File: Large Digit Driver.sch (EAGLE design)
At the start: 25 parts, among them U1 TPIC6B595PTH

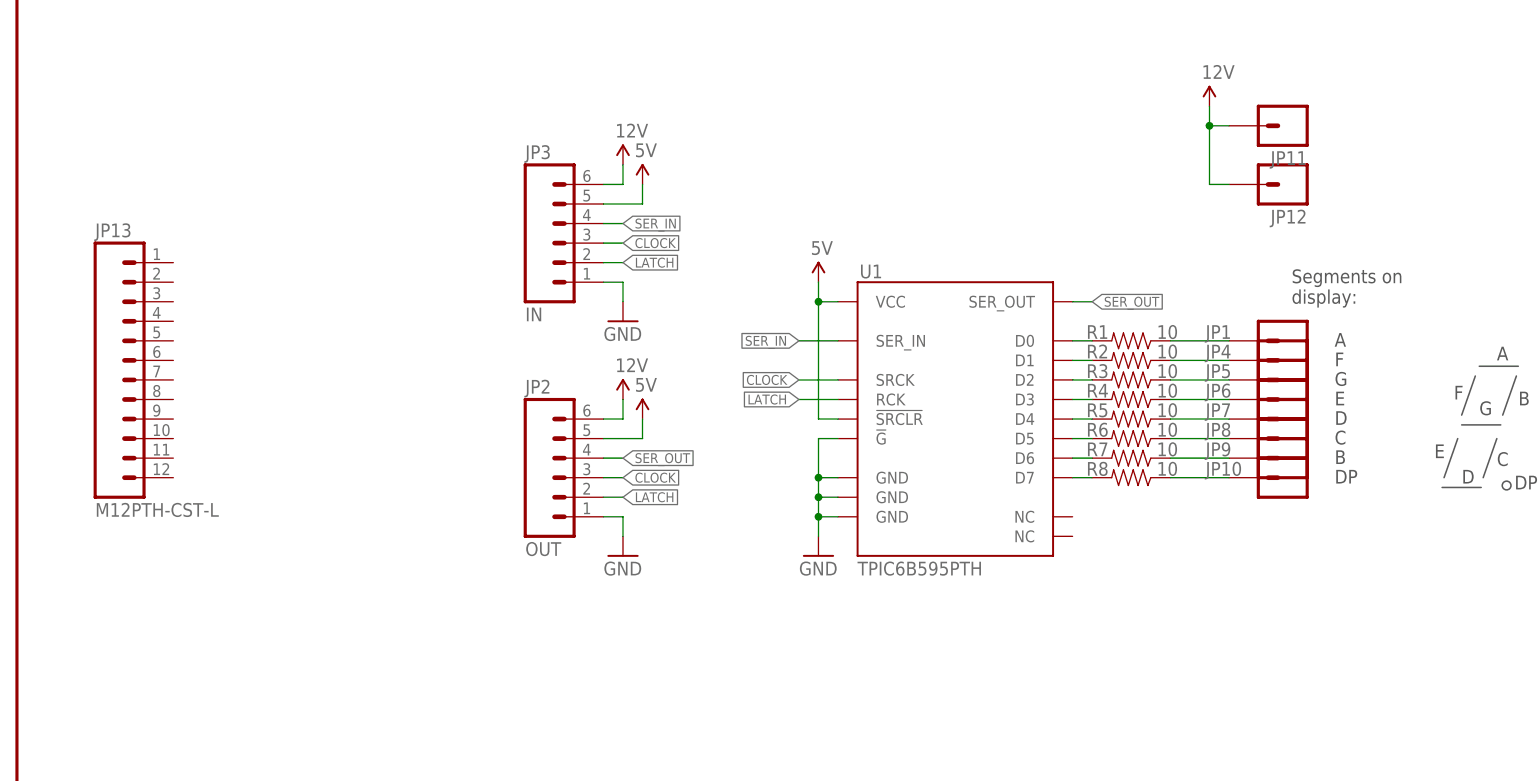
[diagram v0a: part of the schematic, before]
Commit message: Conversion to SMD parts.
Board is much smaller. Uses TPIC6C596.
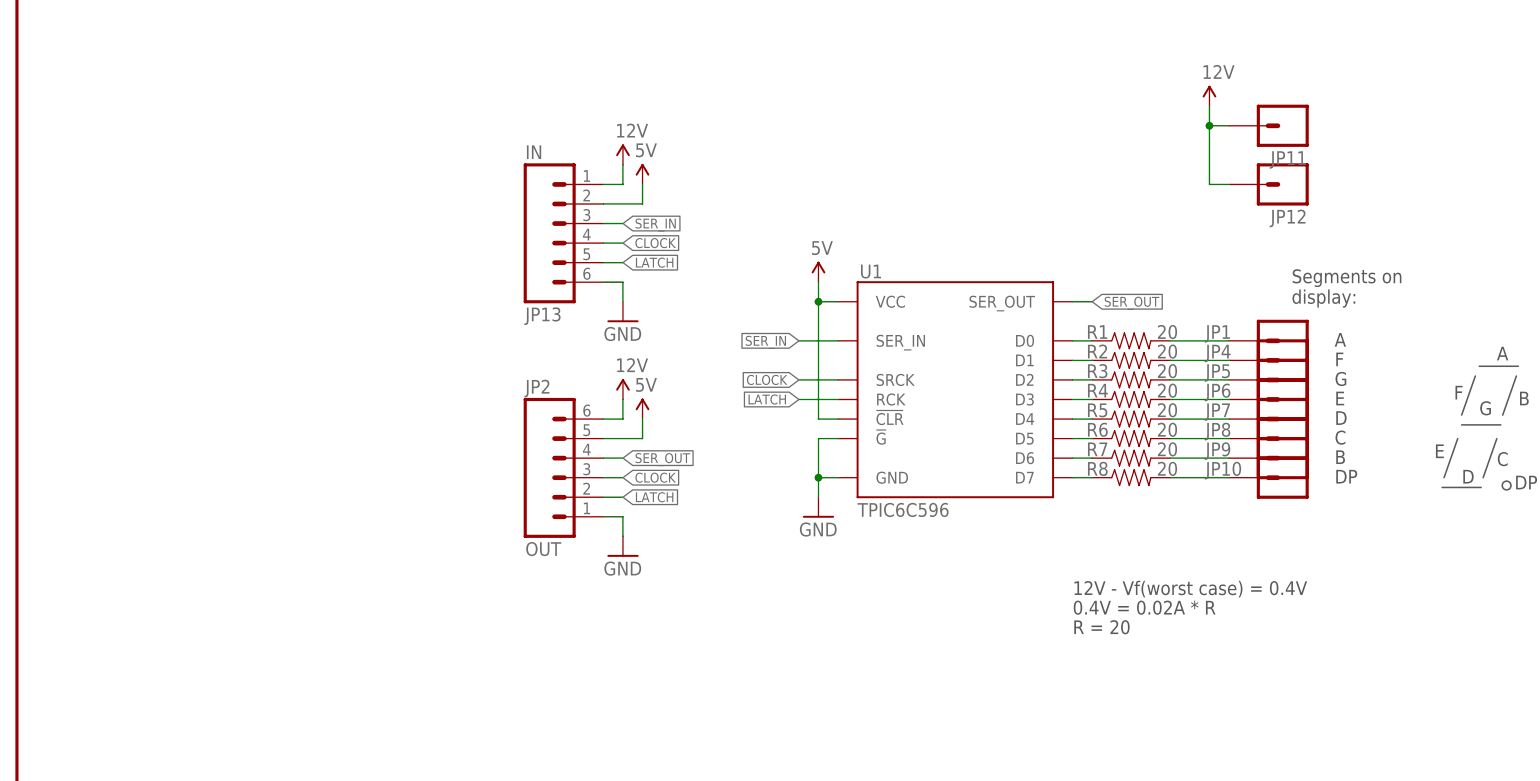
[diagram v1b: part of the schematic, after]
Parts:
- removed JP3: IN, SparkFun-Connectors:M06SILK_FEMALE_PTH
- JP13: value M12PTH-CST-L -> IN; device Spark:M12PTH-CST-L -> SparkFun-Connectors:M06SMD
- JP2: device SparkFun-Connectors:M06SILK_FEMALE_PTH -> SparkFun-Connectors:M06SMD
- R1, R2, R3, R4, R5, R6, R7, R8: value 10 -> 20; device SparkFun-Resistors:1KOHM-1/4W-1%(PTH) -> SparkFun-Resistors:20OHM1/10W1%(0603)SMD
- U1: value TPIC6B595PTH -> TPIC6C596; device SparkFun-DigitalIC:TPIC6B595PTH -> SparkFun-DigitalIC:TPIC6C596SOIC
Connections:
- net 12V: now also JP13.1; no longer JP3.6
- net 5V: now also JP13.2, U1.!CLR; no longer JP3.5, U1.!SRCLR
- net CLOCK: now also JP13.4; no longer JP3.3
- net D0: now also R1.1; no longer R1.2
- net D1: now also R2.1; no longer R2.2
- net D2: now also R3.1; no longer R3.2
- net D3: now also R4.1; no longer R4.2
- net D4: now also R5.1; no longer R5.2
- net D5: now also R6.1; no longer R6.2
- net D6: now also R7.1; no longer R7.2
- net D7: now also R8.1; no longer R8.2
- net GND: now also JP13.6, U1.GND; no longer JP3.1, U1.GND@10, U1.GND@11, U1.GND@19
- net LATCH: now also JP13.5; no longer JP3.2
- net S0: now also R1.2; no longer R1.1
- net S1: now also R2.2; no longer R2.1
- net S2: now also R3.2; no longer R3.1
- net S3: now also R4.2; no longer R4.1
- net S4: now also R5.2; no longer R5.1
- net S5: now also R6.2; no longer R6.1
- net S6: now also R7.2; no longer R7.1
- net S7: now also R8.2; no longer R8.1
- net SER_IN: now also JP13.3; no longer JP3.4
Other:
- note added: "0.4V = 0.02A * R"
- note added: "12V - Vf(worst case) = 0.4V"
- note added: "R = 20"
- moved on the sheet: R1, R2, R3, R4, R5, R6, R7, R8

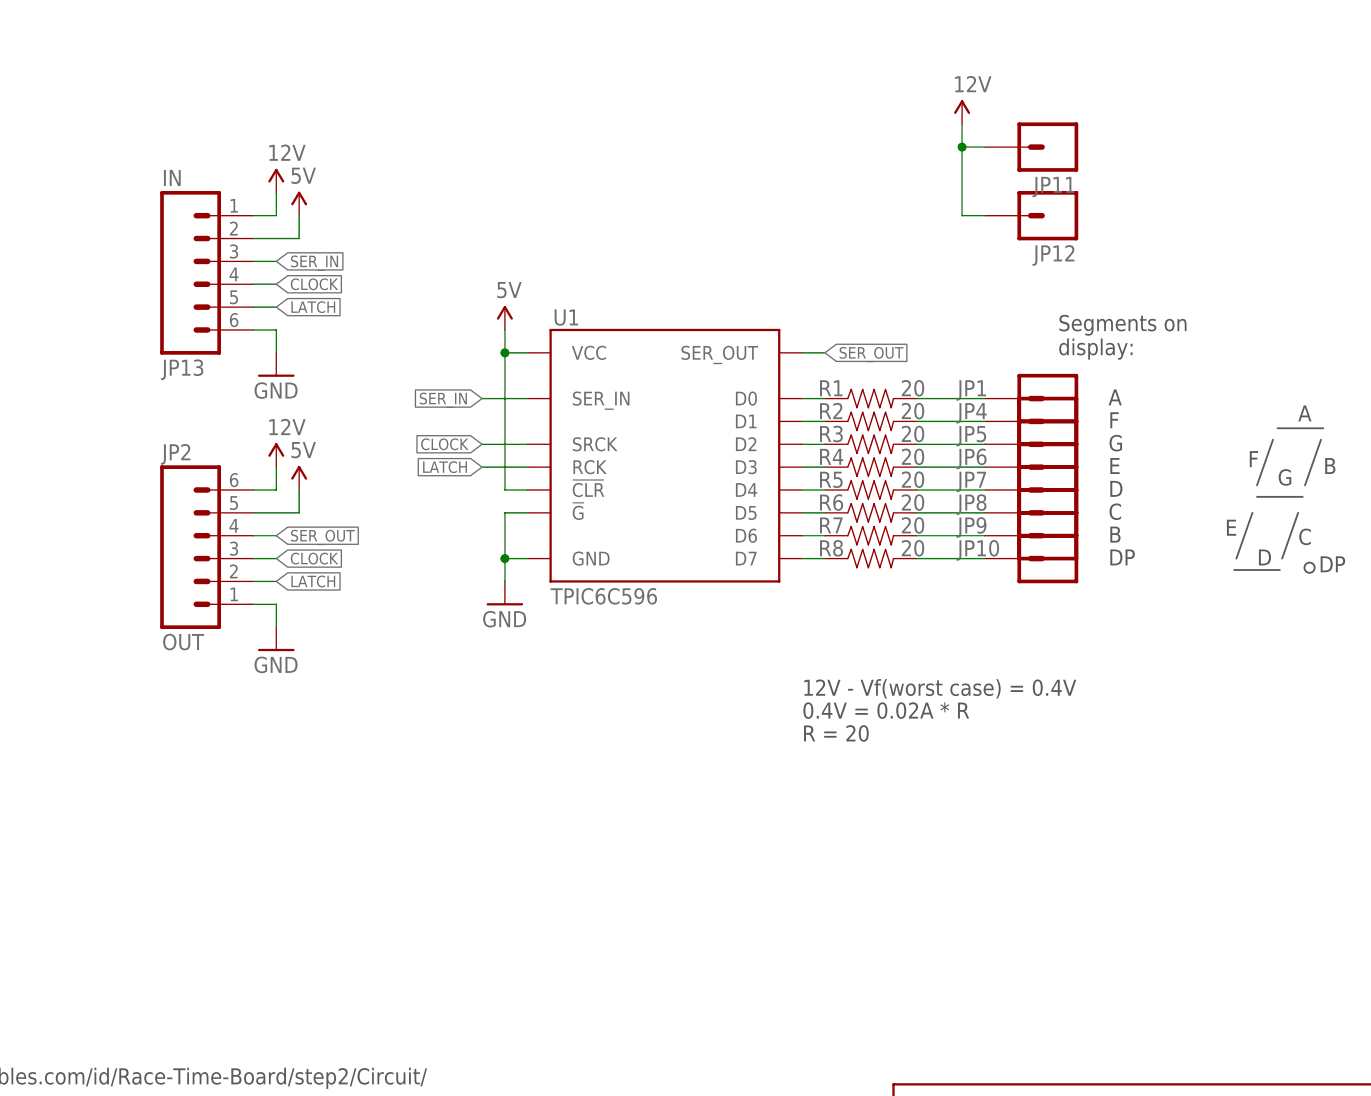
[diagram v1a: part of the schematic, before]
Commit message: Adding anchor pins for SMD mounting.
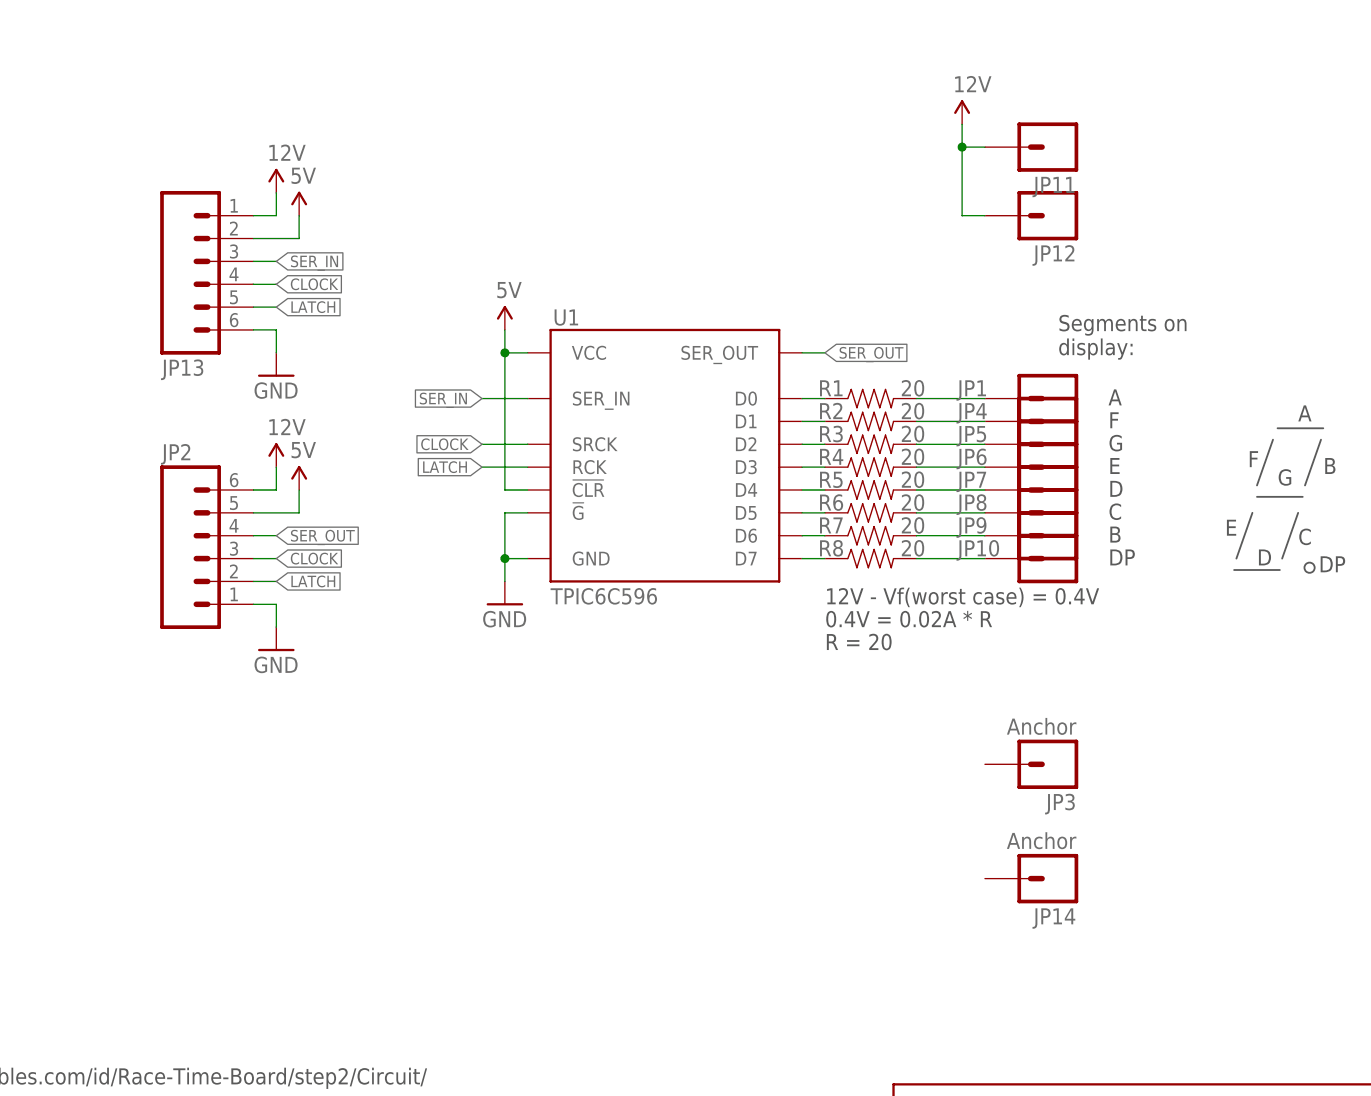
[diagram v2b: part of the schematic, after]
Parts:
- added JP14, JP3: Anchor, SparkFun-Connectors:M01PTH_LONGPAD
- JP13: value IN -> (none)
- JP2: value OUT -> (none)
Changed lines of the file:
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@@
 <?xml version="1.0" encoding="utf-8"?>
 <!DOCTYPE eagle SYSTEM "eagle.dtd">
-<eagle version="7.1.0">
+<eagle version="7.2.0">
 <drawing>
 <settings>
@@
 <part name="GND1" library="SparkFun-Aesthetics" deviceset="GND" device=""/>
 <part name="SUPPLY2" library="SparkFun-Aesthetics" deviceset="5V" device=""/>
-<part name="JP2" library="SparkFun-Connectors" deviceset="M06" device="SMD" value="OUT"/>
+<part name="JP2" library="SparkFun-Connectors" deviceset="M06" device="SMD"/>
 <part name="SUPPLY3" library="SparkFun-Aesthetics" deviceset="5V" device=""/>
 <part name="GND2" library="SparkFun-Aesthetics" deviceset="GND" device=""/>
@@
 <part name="R7" library="SparkFun-Resistors" deviceset="20OHM1/10W1%(0603)" device="SMD" value="20"/>
 <part name="R8" library="SparkFun-Resistors" deviceset="20OHM1/10W1%(0603)" device="SMD" value="20"/>
-<part name="JP13" library="SparkFun-Connectors" deviceset="M06" device="SMD" value="IN"/>
+<part name="JP13" library="SparkFun-Connectors" deviceset="M06" device="SMD"/>
 <part name="U1" library="SparkFun-DigitalIC" deviceset="TPIC6C596" device="SOIC" value="TPIC6C596"/>
+<part name="JP3" library="SparkFun-Connectors" deviceset="M01" device="PTH_LONGPAD" value="Anchor"/>
+<part name="JP14" library="SparkFun-Connectors" deviceset="M01" device="PTH_LONGPAD" value="Anchor"/>
 </parts>
 <sheets>
@@
 <text x="165.608" y="116.586" size="1.778" layer="97">Segments on
 display:</text>
-<text x="137.16" y="78.74" size="1.778" layer="97">12V - Vf(worst case) = 0.4V</text>
-<text x="137.16" y="76.2" size="1.778" layer="97">0.4V = 0.02A * R</text>
-<text x="137.16" y="73.66" size="1.778" layer="97">R = 20</text>
+<text x="139.7" y="88.9" size="1.778" layer="97">12V - Vf(worst case) = 0.4V</text>
+<text x="139.7" y="86.36" size="1.778" layer="97">0.4V = 0.02A * R</text>
+<text x="139.7" y="83.82" size="1.778" layer="97">R = 20</text>
 </plain>
 <instances>
@@
 <instance part="JP13" gate="G$1" x="71.12" y="127" rot="MR180"/>
 <instance part="U1" gate="U1" x="121.92" y="106.68"/>
+<instance part="JP3" gate="G$1" x="165.1" y="71.12" rot="R180"/>
+<instance part="JP14" gate="G$1" x="165.1" y="58.42" rot="R180"/>
 </instances>
 <busses>

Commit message: Added fiducials for issue #1.
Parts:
- added FID1, FID2: FIDUCIAL1X2, SparkFun-Aesthetics:FIDUCIAL1X2
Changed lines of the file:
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@@
 <part name="JP3" library="SparkFun-Connectors" deviceset="M01" device="PTH_LONGPAD" value="Anchor"/>
 <part name="JP14" library="SparkFun-Connectors" deviceset="M01" device="PTH_LONGPAD" value="Anchor"/>
+<part name="FID1" library="SparkFun-Aesthetics" deviceset="FIDUCIAL" device="1X2"/>
+<part name="FID2" library="SparkFun-Aesthetics" deviceset="FIDUCIAL" device="1X2"/>
 </parts>
 <sheets>
@@
 <instance part="JP3" gate="G$1" x="165.1" y="71.12" rot="R180"/>
 <instance part="JP14" gate="G$1" x="165.1" y="58.42" rot="R180"/>
+<instance part="FID1" gate="G$1" x="246.38" y="20.32"/>
+<instance part="FID2" gate="G$1" x="241.3" y="20.32"/>
 </instances>
 <busses>

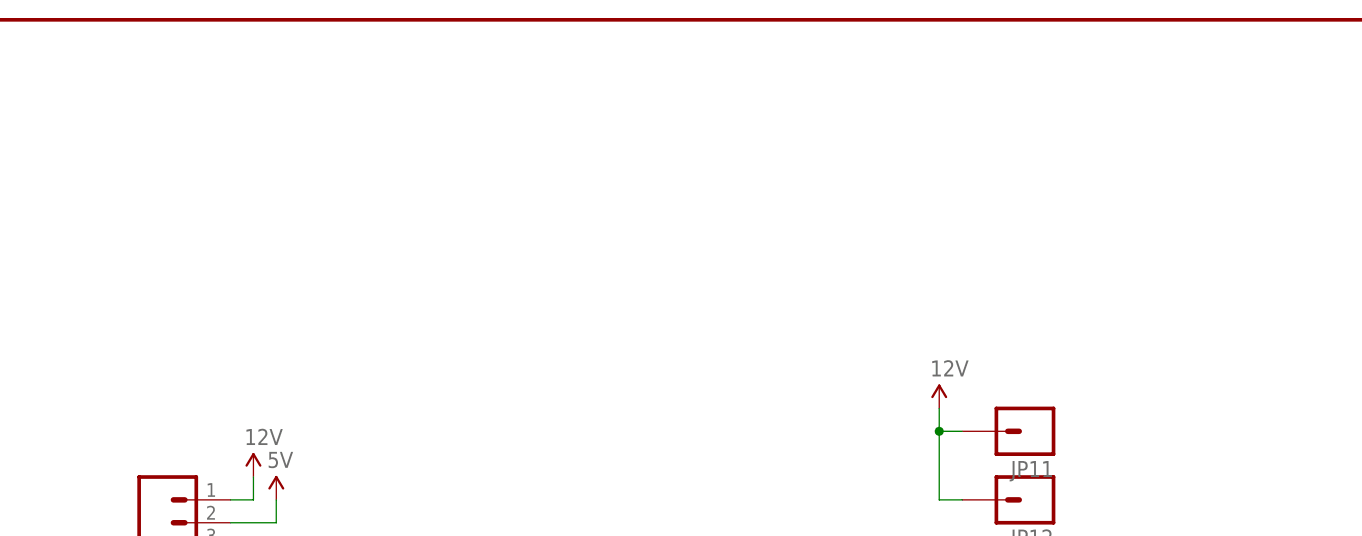
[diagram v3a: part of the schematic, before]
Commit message: Note added to schematic: issue #2
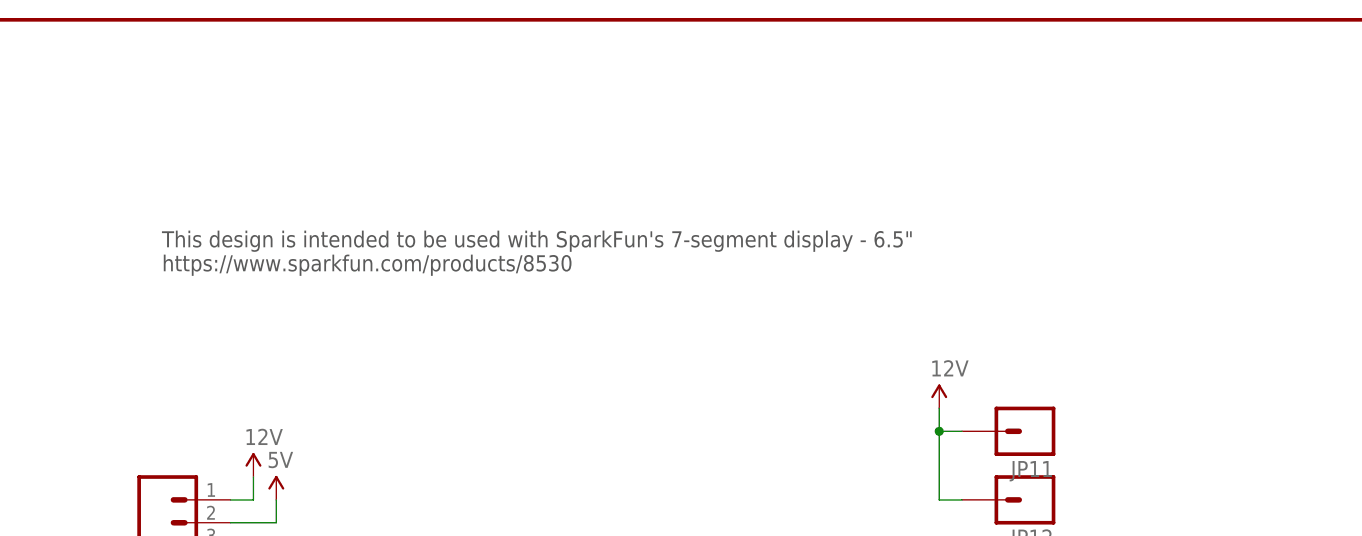
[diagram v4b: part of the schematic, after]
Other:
- note added: "This design is intended to be used with SparkFun's 7-segment display - 6.5" https://www.sparkfun.com/products/8530"
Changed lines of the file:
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@@
 <text x="139.7" y="86.36" size="1.778" layer="97">0.4V = 0.02A * R</text>
 <text x="139.7" y="83.82" size="1.778" layer="97">R = 20</text>
+<text x="68.58" y="157.48" size="1.778" layer="97">This design is intended to be used with SparkFun's 7-segment display - 6.5"
+https://www.sparkfun.com/products/8530</text>
 </plain>
 <instances>
